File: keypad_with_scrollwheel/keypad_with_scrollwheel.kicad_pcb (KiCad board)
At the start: 2 copper layers, 40 x 60 mm, 32 parts

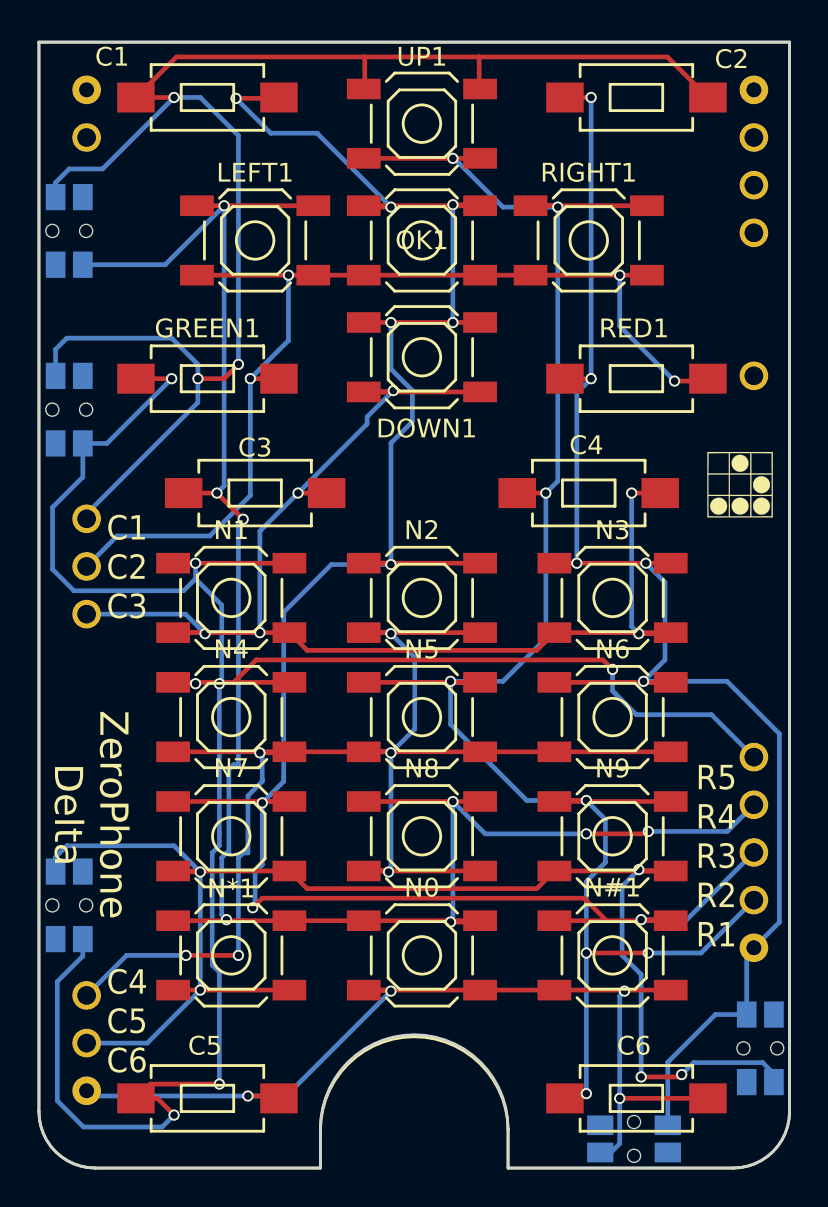
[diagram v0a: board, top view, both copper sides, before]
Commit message: Finished the keypad+scrollwheel board - needs to be printed out
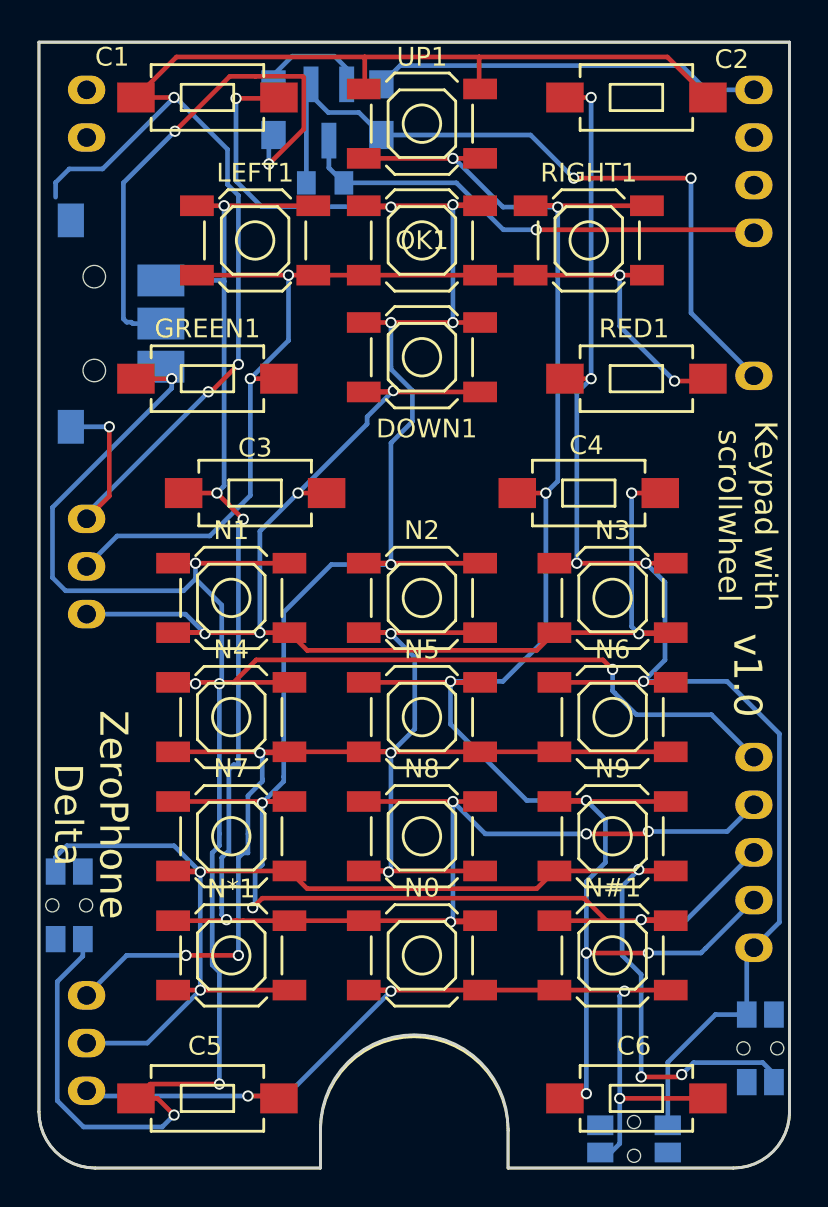
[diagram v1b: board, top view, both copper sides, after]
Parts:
- removed ?: KEYPAD_OVERLAY, common_footprints:keypad_overlay
- removed G***: LOGO, art:glider
- removed VOL_DOWN1, VOL_UP1: AB2_SWITCH_MOMENTARY, footprints:SW_SPST_EVQP7C
- added C7: 100nF, Capacitors_SMD:C_0805, B.Cu at (163.8, 112.5)
- added Q1: BC847, TO_SOT_Packages_SMD:SOT-23_Handsoldering, B.Cu at (163.9, 108.8)
- added R1: 1K, Resistors_SMD:R_0805_HandSoldering, B.Cu at (161.0, 108.6)
- added R2: 10K, Resistors_SMD:R_0805_HandSoldering, B.Cu at (166.8, 108.6)
- added U1: KEYPAD_OVERLAY, footprints:keypad_overlay, F.Cu at (148.5, 105.0)
- added U2: SCROLLWHEEL, footprints:SCROLLWHEEL, B.Cu at (150.2, 120.0)
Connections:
- net /COL1 renamed COM
- net /ROW4 renamed LEFT
- net /ROW5 renamed RIGHT
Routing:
- net GPIO: track 0.00 -> 39.9 mm, vias 0 -> 2
- net PUSH: track 0.00 -> 28.4 mm, vias 0 -> 2
- net GND: track 0.00 -> 25.5 mm, vias 0 -> 1
- net +3V3: track 0.00 -> 20.8 mm
- net Net-(Q1-Pad2): track 0.00 -> 5.93 mm
- net LEFT: track 104.6 -> 99.8 mm
- net COM: track 86.2 -> 81.5 mm, vias 3 -> 4
- net /ROW3: track 121.8 -> 124.4 mm
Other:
- board text added: "BC847"
- board text added: "For assembly, follow directions for the normal keypad boards (available in assembly instructions) Values for SMD resistors/ capacitors are yet to be determined"
- board text added: "Keypad board with scrollwheel v1.0, by CRImier"
- board text added: "Keypad with scrollwheel"
- board text added: "Serial number"
- board text added: "v1.0"
- board text removed: "1. Solder 4-pin buttons in the center row 2. Solder first and third rows of 4-pin buttons 3. Solder 2-pin buttons 4. Flip the board, solder side buttons (you can tack them on with superglue first) 5. Solder the headers on, facing downwards"
- board text removed: "C1 C2 C3"
- board text removed: "C4 C5 C6"
- board text removed: "If you're soldering SMD parts yourself, this might be the board to work on first. Solder one pad of the button on, adjust the button, solder the other pads, repeat."
- board text removed: "R5 R4 R3 R2 R1"
